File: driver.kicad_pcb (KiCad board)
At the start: 2 copper layers, 53.8 x 69.1 mm, 45 parts, among them J1 Screw_Terminal_01x02, J2 Conn_02x12_Odd_Even, Q10 Q_NMOS_GDSD, Q11 Q_NMOS_GDSD, Q12 Q_NMOS_GDSD, Q13 Q_NMOS_GDSD, Q14 Q_NMOS_GDSD, Q15 Q_NMOS_GDSD, Q16 Q_NMOS_GDSD, Q17 IRF9Z34 PMOS_DGS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

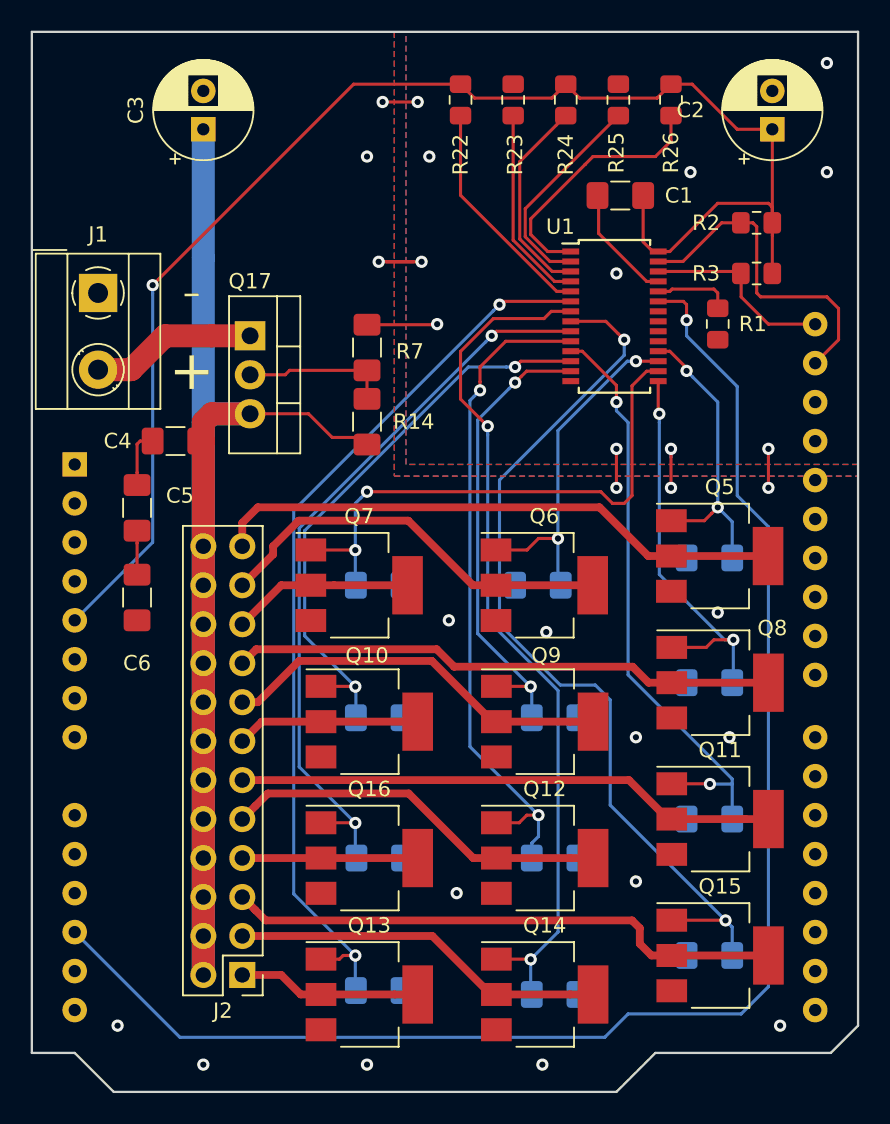
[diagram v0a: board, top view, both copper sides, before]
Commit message: update for mosfet pinout change
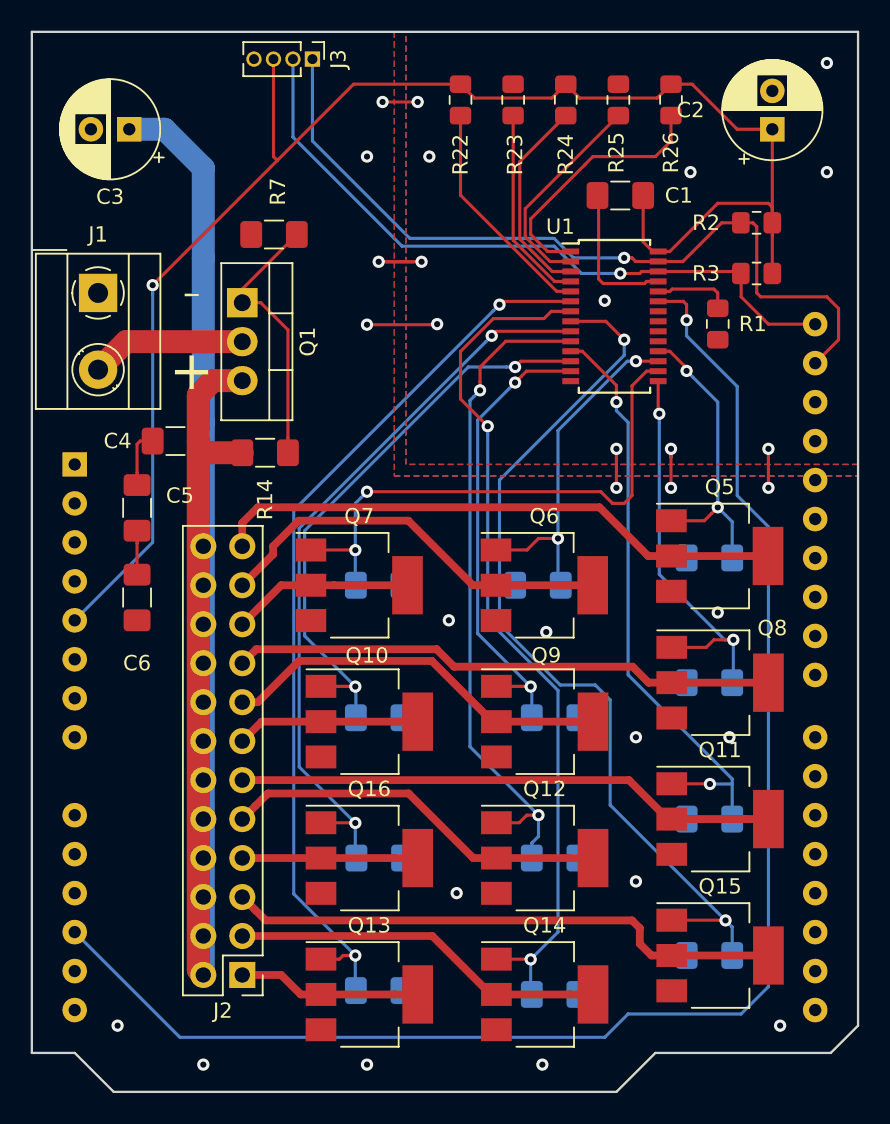
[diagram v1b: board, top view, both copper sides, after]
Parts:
- removed Q17: IRF9Z34 PMOS_DGS, Package_TO_SOT_THT:TO-220-3_Vertical
- added J3: Conn_01x04_Male, Connector_PinHeader_1.27mm:PinHeader_1x04_P1.27mm_Vertical, F.Cu at (93.5, 74.9)
- added Q1: IRF9Z34 PMOS_GDS, Package_TO_SOT_THT:TO-220-3_Vertical, F.Cu at (88.9, 90.8)
- moved R7 9.54 mm to (91.0, 86.4), turned to 180 degrees
- moved R14 6.94 mm to (90.4, 100.6), turned to 0 degrees
- moved C3 4.83 mm to (81.5, 79.5), turned to 180 degrees
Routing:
- net /SCL: track 12.5 -> 45.2 mm, vias 0 -> 1
- net /SDA: track 21.8 -> 53.0 mm, vias 0 -> 1
- net Net-(Q1-Pad1): track 10.1 -> 17.6 mm
- net VCC: track 96.0 -> 102.7 mm
- net 28V: track 106.0 -> 102.5 mm
- net GND: track 27.0 -> 28.9 mm, vias 29 -> 30
- net /input_hicurrent: track 10.8 -> 10.2 mm

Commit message: ITLL design rule tolerances and sizes, neccesistated a full re-routing of all traces
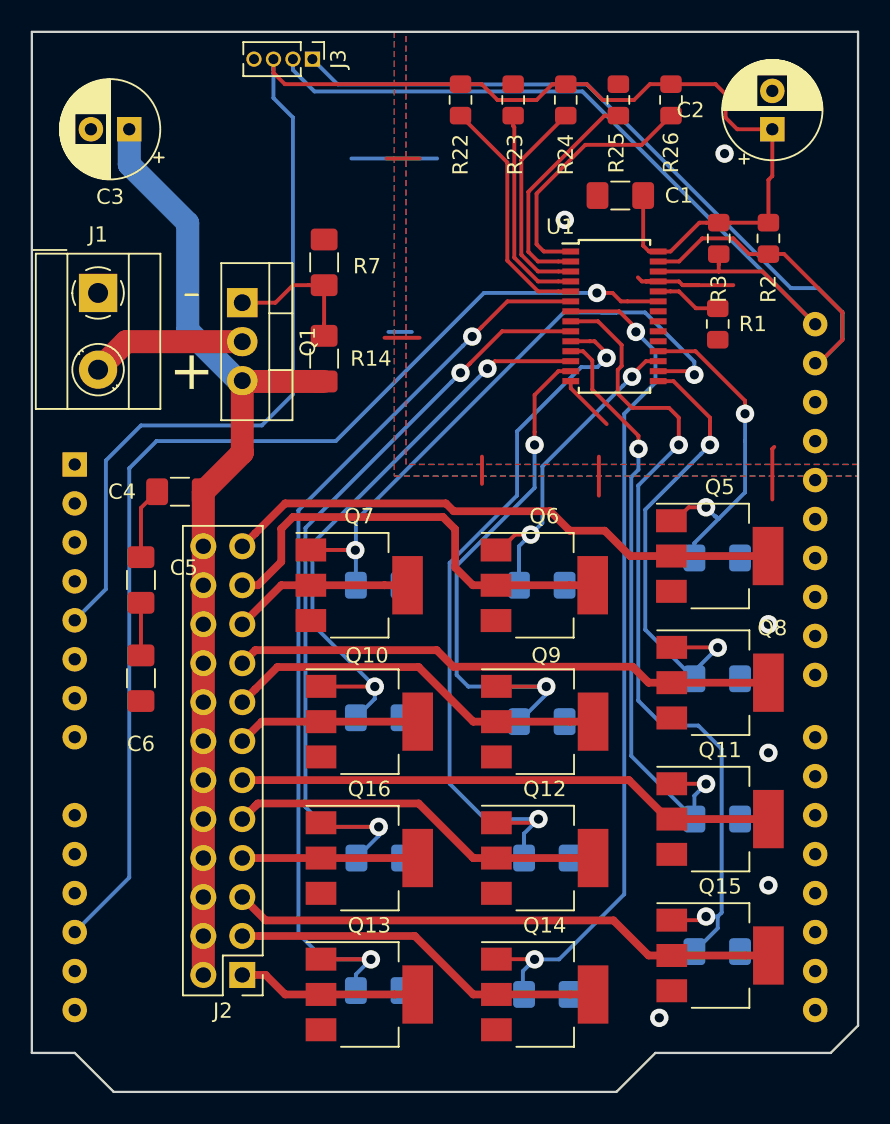
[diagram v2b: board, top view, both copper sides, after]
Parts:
- moved R14 7.24 mm to (94.2, 94.5), turned to 90 degrees
- moved C6 5.27 mm to (82.3, 115.3)
- moved C5 4.71 mm to (82.3, 108.9)
- moved R7 3.74 mm to (94.2, 88.2), turned to 90 degrees
- moved R3 3.36 mm to (120.0, 86.6), turned to 270 degrees
- moved C4 3.31 mm to (84.8, 103.1)
- moved R2 1.28 mm to (123.2, 86.6), turned to 270 degrees
- moved R13 0.87 mm to (108.4, 118.1)
- moved R21 0.57 mm to (119.9, 115.3), turned to 0 degrees
- moved R6 0.57 mm to (119.9, 133.1), turned to 0 degrees
- moved R10 0.51 mm to (108.7, 127.0)
- moved R11 0.51 mm to (119.9, 124.5), turned to 0 degrees
- moved R18 0.51 mm to (119.9, 107.4), turned to 0 degrees
- moved R5 0.51 mm to (108.7, 135.9)
- moved R19 0.25 mm to (108.4, 109.2), turned to 0 degrees
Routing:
- net 28V: track 102.5 -> 64.7 mm
- net /~OE: track 98.0 -> 71.1 mm
- net /SDA: track 53.0 -> 64.4 mm, vias 1 -> 0
- net /SCL: track 45.2 -> 54.4 mm, vias 1 -> 0
- net Net-(Q1-Pad1): track 17.6 -> 9.11 mm
- net /PWM7: track 30.5 -> 35.8 mm
- net /PWM3: track 48.3 -> 52.6 mm
- net /PWM4: track 43.9 -> 48.1 mm
- net /PWM9: track 36.4 -> 40.5 mm
- net /PWM8: track 26.3 -> 30.1 mm
- net /PWM2: track 58.6 -> 55.2 mm
- net /PWM11: track 19.3 -> 22.4 mm
- net /PWM0: track 59.3 -> 62.1 mm
- net PWR_CH10: track 26.6 -> 29.2 mm
- net GND: track 28.9 -> 31.4 mm, vias 30 -> 6
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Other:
- net class Default: clearance 0.1524 -> 0.2032; trace_width 0.2032 -> 0.254; via_dia 0.8 -> 1.2; via_drill 0.4 -> 0.6
- rule trace_clearance: 0.1524 -> 0.2032
